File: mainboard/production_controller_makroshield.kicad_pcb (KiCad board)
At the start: 2 copper layers, 165.1 x 204 mm, 112 parts, among them J1 CON_TERM_BLK_1X2_TB008A-508-0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, J10 CON_CONNAXIO_MOTOR_DRIVER, J11 CON_CONNAXIO_MOTOR_DRIVER, J12 CON_CONNAXIO_MOTOR_DRIVER, J13 CON_CONNAXIO_MOTOR_DRIVER, J14 CON_CONNAXIO_MOTOR_DRIVER, J15 CON_CONNAXIO_MOTOR_DRIVER, J16 CON_CONNAXIO_MOTOR_DRIVER, J17 CON_CONNAXIO_MOTOR_DRIVER, J18 CON_CONNAXIO_MOTOR_DRIVER, J19 CON_CONNAXIO_MOTOR_DRIVER, J2 CON_TERM_BLK_1X2_TB008A-508-0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, J20 CON_CONNAXIO_MOTOR_DRIVER, J21 CON_CONNAXIO_MOTOR_DRIVER, J3 CON_HDR_MIKROBUS_ADDON_TH, J4 CON_TERM_BLK_1X2_TB008A-508-0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, J5 CON_HDR_MIKROBUS_SOCKET_TH, J6 CON_HDR_100MILS_M_TH_1X3, J7 CON_CONNAXIO_MOTOR_DRIVER, J8 CON_CONNAXIO_MOTOR_DRIVER, J9 CON_CONNAXIO_MOTOR_DRIVER, Q1 TRX_PMOS_AOD4189, Q2 TRX_2NPN_BC846S,115, U1 IO_EXP_PI4IOE5V6416ZDEX, U2 IO_EXP_PI4IOE5V6416ZDEX, U3 SEN_TEMP_TMP1075DR, U4 SEN_CUR_ACS711KEXLT-31AB-T, U5 ADC_NAU7802SGI

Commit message: Add filter cap to current reading ADC
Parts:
- added C11: CAP_CER_100NF_25V_0402, connaxio-capacitors:CAP_CER_0402_1005M, F.Cu at (145.5, 198.8)
- moved C14 1.09 mm to (145.5, 201.1), turned to -90 degrees
- renumbered C11 to C12, C12 to C13, C13 to C14, C14 to C15
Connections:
- U5 pad 4: GND -> Net-(U5-Pad4)
- U5 pad 5: GND -> Net-(U5-Pad5)
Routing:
- net Net-(U5-Pad4): track 0.00 -> 2.09 mm
- net GND: track 297.3 -> 295.3 mm, vias 345 -> 342
- net Net-(U5-Pad5): track 0.00 -> 1.98 mm

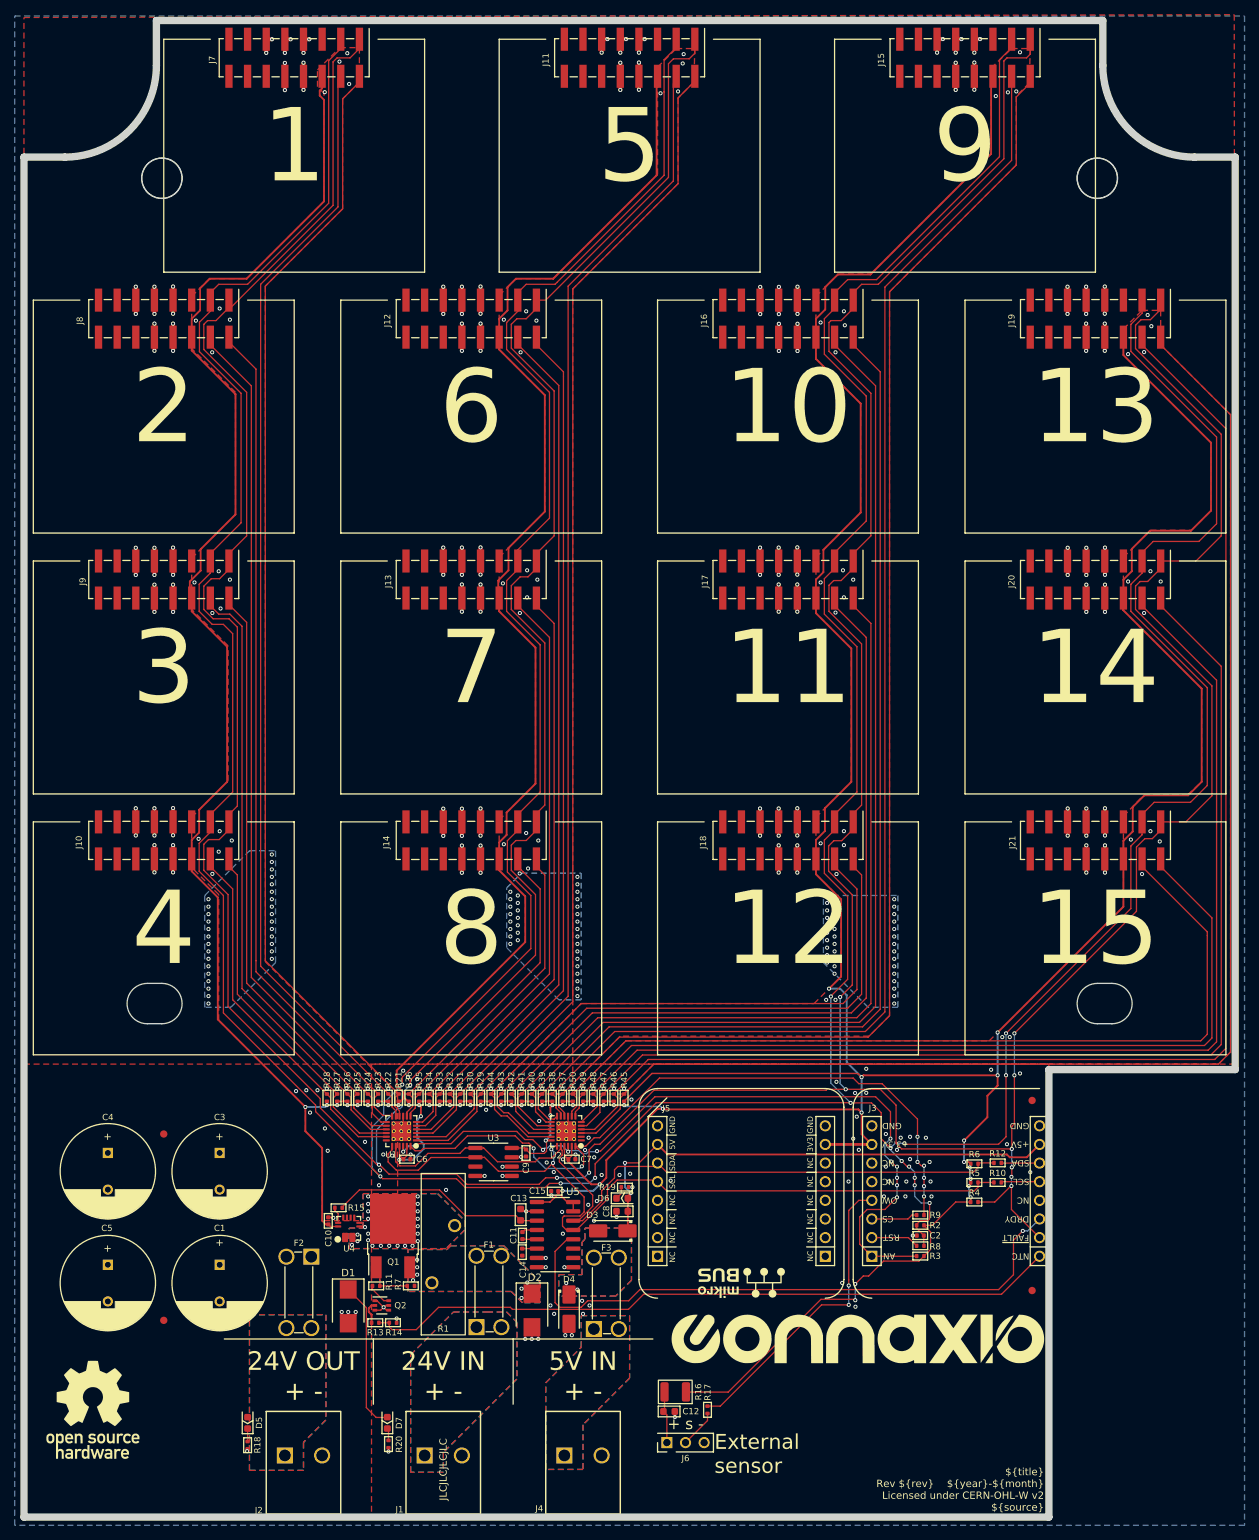
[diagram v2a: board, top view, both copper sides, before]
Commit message: Add 4 extra IOs (SVG connectors)
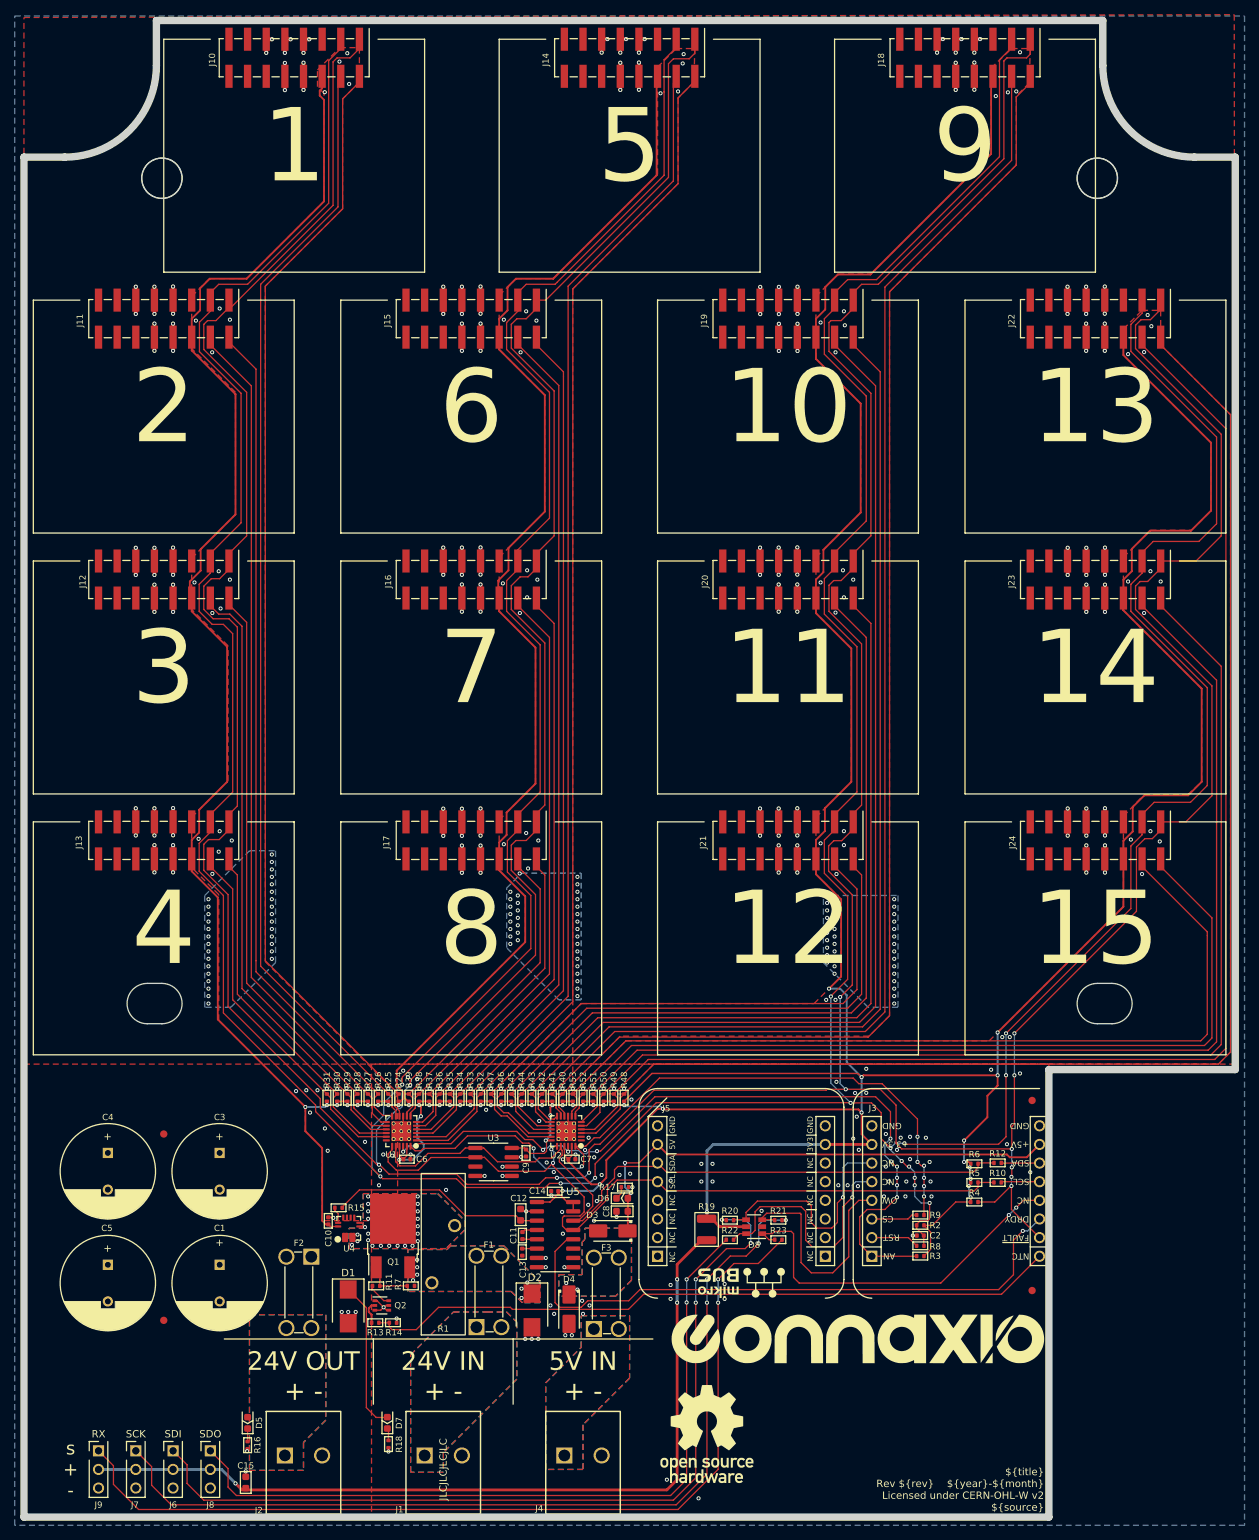
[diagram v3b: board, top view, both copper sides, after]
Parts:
- removed the R16 at (166.3, 220.1)
- added D8: DIO_TVS_SRV05-4HTG, connaxio-sop:SOT-23-6, F.Cu at (177.1, 197.6)
- added J6: CON_HDR_100MILS_M_TH_1X3, connaxio-connectors:CON_HDR_100MILS_M_TH_1X3, F.Cu at (97.9, 230.7)
- added J8: CON_HDR_100MILS_M_TH_1X3, connaxio-connectors:CON_HDR_100MILS_M_TH_1X3, F.Cu at (103.0, 230.7)
- added J9: CON_HDR_100MILS_M_TH_1X3, connaxio-connectors:CON_HDR_100MILS_M_TH_1X3, F.Cu at (87.7, 230.7)
- added R19: PTC_SMD1210B010TF, connaxio-resistors:RES_1210_3225M, F.Cu at (170.6, 198.0)
- added R20: RES_226Ω_1%_0402, connaxio-resistors:RES_0402_1005M, F.Cu at (173.8, 196.7)
- added R22: RES_226Ω_1%_0402, connaxio-resistors:RES_0402_1005M, F.Cu at (173.8, 199.4)
- added R23: RES_226Ω_1%_0402, connaxio-resistors:RES_0402_1005M, F.Cu at (180.4, 199.4)
- moved G*** 83.8 mm to (170.7, 225.9)
- moved J7 75.0 mm to (92.8, 230.7), turned to 0 degrees
- moved C15 58.5 mm to (107.8, 232.5), turned to 90 degrees
- moved R21 27.6 mm to (180.4, 196.7), turned to 0 degrees
- renumbered C13 to C12, C14 to C13, C15 to C14, C12 to C15, J7 to J10, J8 to J11, J9 to J12, J10 to J13, J11 to J14, J12 to J15, J13 to J16, J14 to J17, J15 to J18, J16 to J19, J17 to J20, J18 to J21, J19 to J22, J20 to J23, J21 to J24, J6 to J7, R18 to R16, R19 to R17, R20 to R18, R17 to R21, R21 to R24, R22 to R25, R23 to R26, R24 to R27, R25 to R28, R26 to R29, R27 to R30, R28 to R31, R29 to R32, R30 to R33, R31 to R34, R32 to R35, R33 to R36, R34 to R37, R35 to R38, R36 to R39, R37 to R40, R38 to R41, R39 to R42, R40 to R43, R41 to R44, R42 to R45, R43 to R46, R44 to R47, R45 to R48, R46 to R49, R47 to R50, R48 to R51, R49 to R52, R50 to R53
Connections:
- net /ONE_WIRE renamed /IO_SCK
- C15 pad 1: Net-(C12-Pad1) (its old number) -> Net-(J8-Pad2)
- J3 pad 12: unconnected-(J3-Pad12) -> /IO_RX
- J3 pad 5: unconnected-(J3-Pad5) -> /IO_SDO
- J3 pad 6: unconnected-(J3-Pad6) -> /IO_SDI
- J7 pad 1: Net-(C12-Pad1) (its old number) -> Net-(J7-Pad1)
- J7 pad 2: Net-(J6-Pad2) -> Net-(J8-Pad2)
- R21 pad 2: Net-(J6-Pad2) -> Net-(J7-Pad1)
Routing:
- net Net-(J9-Pad1): track 0.00 -> 128.4 mm, vias 0 -> 2
- net Net-(J7-Pad1): track 0.00 -> 126.8 mm, vias 0 -> 4
- net Net-(J6-Pad1): track 0.00 -> 120.7 mm, vias 0 -> 4
- net Net-(J8-Pad2): track 0.00 -> 115.3 mm, vias 0 -> 3
- net Net-(J8-Pad1): track 0.00 -> 104.8 mm, vias 0 -> 2
- net /IO_RX: track 0.00 -> 51.1 mm, vias 0 -> 2
- net /IO_SDO: track 0.00 -> 33.9 mm, vias 0 -> 1
- net /IO_SDI: track 0.00 -> 31.0 mm, vias 0 -> 1
- net +3.3V: track 950.9 -> 941.0 mm, vias 51 -> 50
- net /IO_SCK: track 41.6 -> 32.2 mm, vias 2 -> 0
- net Net-(C12-Pad1) (its old number): track 7.17 -> 0.00 mm
- net Net-(J6-Pad2): track 5.21 -> 0.00 mm
- net GND: track 295.3 -> 296.0 mm, vias 342 -> 353
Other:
- board text added: "RX"
- board text added: "SCK"
- board text added: "SDI"
- board text added: "SDO"
- board text added: "s + -"
- board text removed: "+ s -"
- board text removed: "External sensor"
